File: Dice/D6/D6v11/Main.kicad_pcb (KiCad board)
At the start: 2 copper layers, 68.9 x 50.8 mm, 106 parts, among them J1 Conn_01x14, J2 Conn_01x04, J3 Conn_01x02, P5 COILA, P6 COILB, U1 N52810_QFN32, U2 SC7A20HTR, U3 PJ75BL50SA, U4 ME6230, U5 BL24C02F-NTRC, U6 AW35122, U7 DS6101, U8 SL1605, U9 XT4051, Y1 32MHz 40ppm

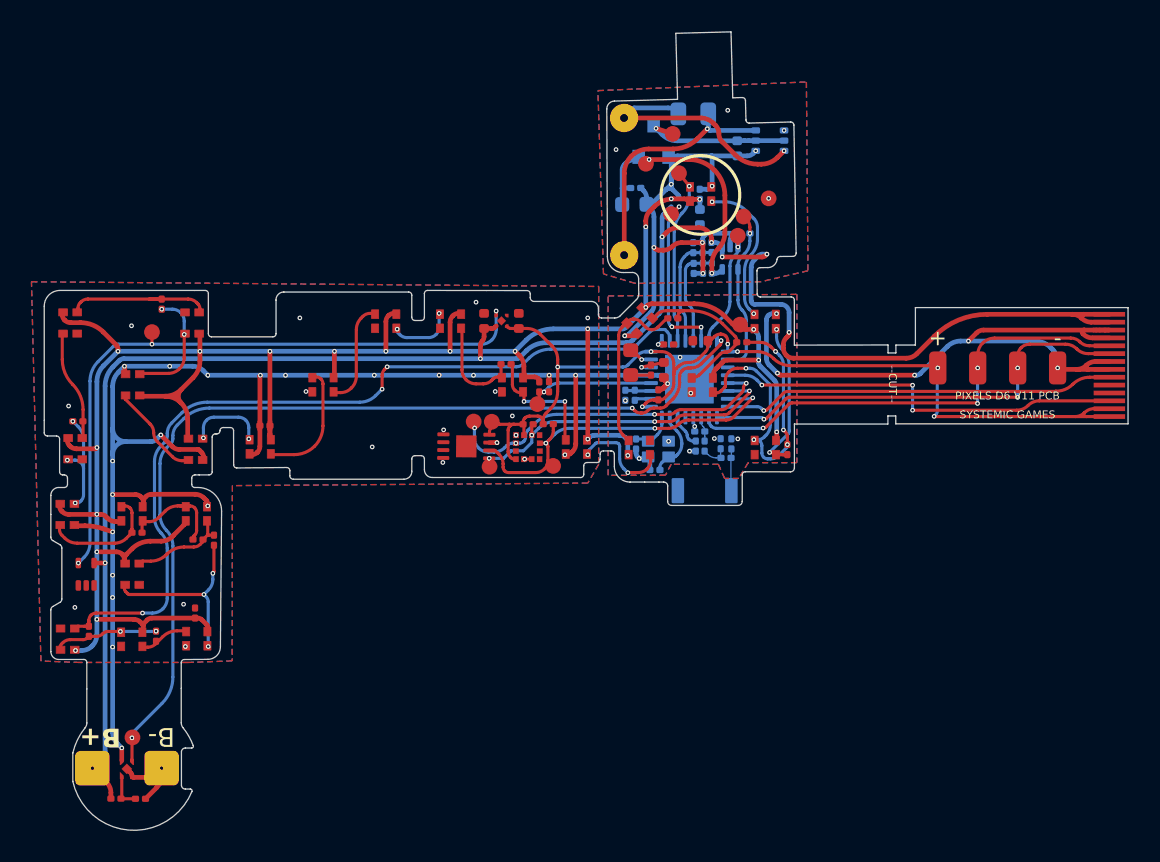
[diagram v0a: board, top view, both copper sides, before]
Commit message: Updated latest FPC versions
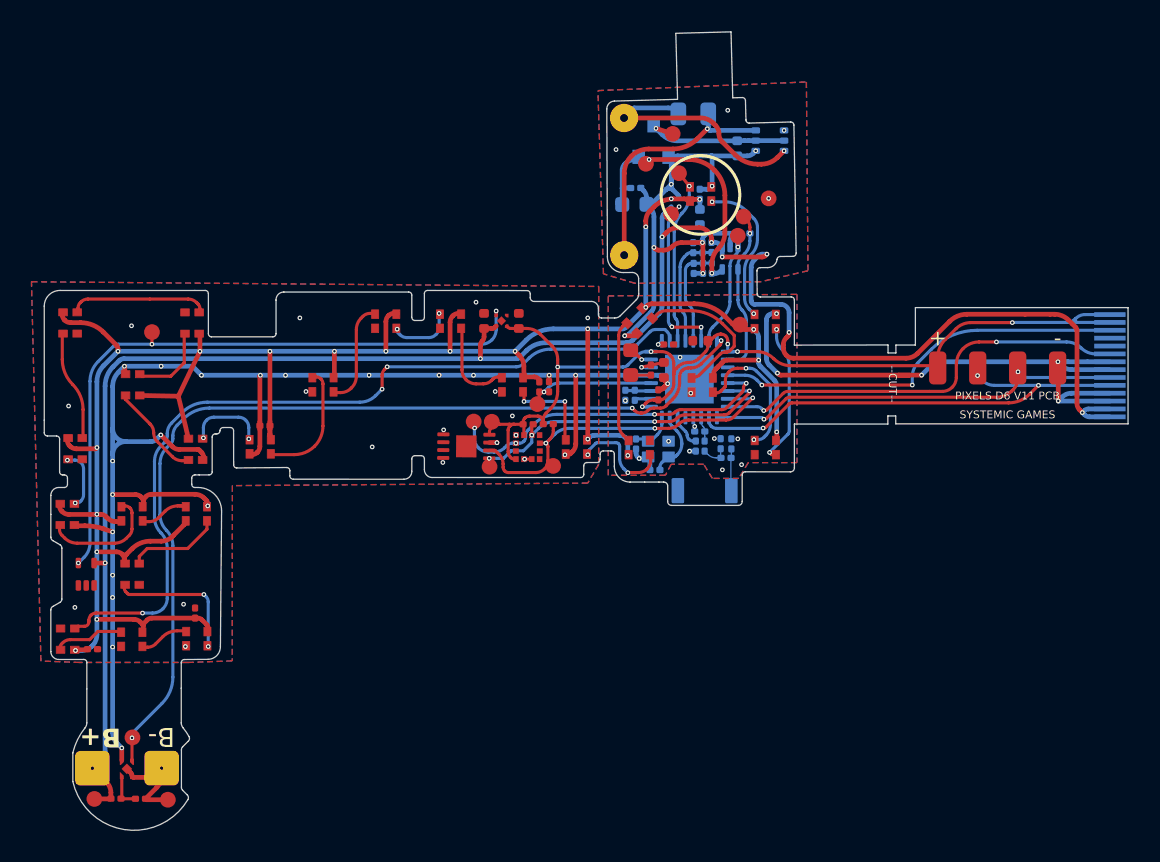
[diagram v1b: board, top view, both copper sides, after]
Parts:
- removed R13, R14, R15, R16, R17, R18, R19, R20, R21, R22, R23: 0R, Resistor_SMD:R_0201_0603Metric
- added C14: 0.1uF 10V 20%, Capacitor_SMD:C_0201_0603Metric, F.Cu at (125.7, 103.8)
- added W14: BATT, Pixels-dice:TEST_PIN, F.Cu at (125.8, 113.3)
- added W24: B-, Pixels-dice:TEST_PIN, F.Cu at (130.5, 113.4)
- J1: moved to B.Cu
- R3: value ~ -> 41.2k 1%
- R6: value 3.9k 1% -> 3.57k 1%
- moved J1 6.52 mm to (190.3, 89.1), turned to 90 degrees
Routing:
- net Net-(D4-DOUT): track 20.7 -> 9.09 mm, vias 5 -> 2
- net +BATT: track 116.5 -> 122.3 mm, vias 7 -> 8
- net Net-(D22-DOUT): track 6.44 -> 2.95 mm
- net Net-(D24-DOUT): track 12.2 -> 8.85 mm, vias 3 -> 2
- net Net-(D20-DOUT): track 7.07 -> 3.83 mm, vias 3 -> 2
- net Net-(D6-DOUT): track 11.0 -> 7.94 mm
- net Net-(D17-DOUT): track 7.51 -> 5.04 mm, vias 2 -> 0
- net GND: track 173.9 -> 171.6 mm, vias 63 -> 65
- net Net-(D8-DOUT): track 7.89 -> 5.62 mm
- net Net-(D26-DOUT): track 6.67 -> 4.48 mm, vias 2 -> 0
- net RESET: track 25.0 -> 27.2 mm, vias 1 -> 2
- net SWDCLK: track 28.7 -> 26.7 mm, vias 3 -> 2
- net Net-(D3-DOUT): track 10.9 -> 9.00 mm
- net VDD: track 66.3 -> 64.5 mm, vias 7 -> 6
- net /Wireless Charging/B-: track 4.56 -> 6.00 mm
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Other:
- outline, holes or cut-outs redrawn
- board text removed: "+"
- board text removed: "-"
- board text removed: "game with pixels .com"
